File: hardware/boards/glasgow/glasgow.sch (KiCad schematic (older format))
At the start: 95 parts, among them J1 USB_C_USB2.0, SW1 RST, U1 CY7C68013A-56LTX, U15 TPD3S014, U2 CAT24M01X, U3 BL24C256A-SFRC, U30 ICE40HX8K-BG121, U36 TLV73312PQDRVR, U7 APX811-40UG-7, U8 TLV75533PDRVR, Y1 24M

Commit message: revC3: Filled in the blanks for the Reset button part number.
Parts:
- SW1: 1b2-bom-key sw-tact-side-tc-1109de -> sw-tact-side-tc-1109de-b-f; MPN TC-1109DE-X-X -> TC-1109DE-B-F
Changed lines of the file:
@@
 F 3 "https://datasheet.lcsc.com/szlcsc/2006061832_XKB-Connectivity-TC-1109DE-C-G_C400325.pdf" H 8400 4300 50  0001 C CNN
 F 4 "XKB" H 8400 4100 50  0001 C CNN "Mfg"
-F 5 "TC-1109DE-X-X" H 8400 4100 50  0001 C CNN "MPN"
-F 6 "sw-tact-side-tc-1109de" H 8400 4100 50  0001 C CNN "1b2-bom-key"
+F 5 "TC-1109DE-B-F" H 8400 4100 50  0001 C CNN "MPN"
+F 6 "sw-tact-side-tc-1109de-b-f" H 8400 4100 50  0001 C CNN "1b2-bom-key"
 	1    8400 4100
 	-1   0    0    -1

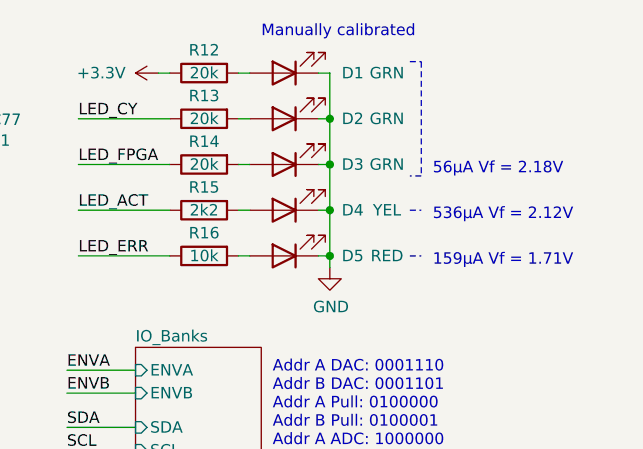
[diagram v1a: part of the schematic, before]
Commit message: revC3: Updated LEDs and current limiting resistors.
* New status LED color scheme: PWR/GRN, FX2/WHT, ICE/BLU, ACT/ORA,
  ERR/RED
* Updated LED part numbers and the corresponding resistor values.
* All LED sourcable from LCSC.
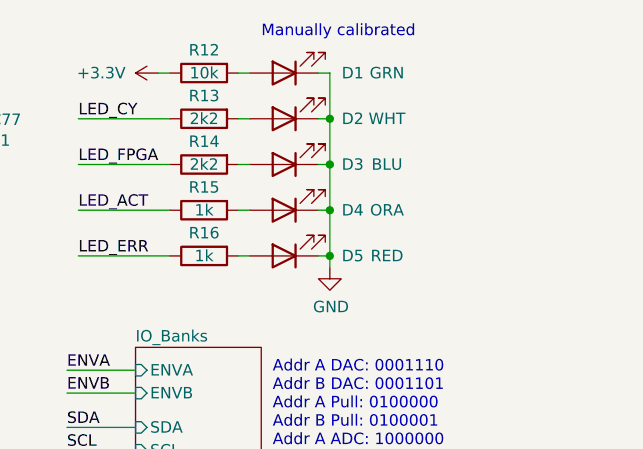
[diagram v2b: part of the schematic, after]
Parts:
- D1: MPN 150060GS75000 -> NCD0603G1; Mfg Wurth Electronics -> Foshan NationStar Optoelectronics
- D2: value GRN -> WHT; 1b2-bom-key led-0603-grn -> led-0603-wht; MPN 150060GS75000 -> NCD0603W1; Mfg Wurth Electronics -> Foshan NationStar Optoelectronics
- D3: value GRN -> BLU; 1b2-bom-key led-0603-grn -> led-0603-blu; MPN 150060GS75000 -> ORH-B36G; Mfg Wurth Electronics -> Orient
- D4: value YEL -> ORA; 1b2-bom-key led-0603-yel -> led-0603-ora; MPN 150060YS75000 -> NCD0603O1; Mfg Wurth Electronics -> Foshan NationStar Optoelectronics
- D5: MPN 150060RS75000 -> NCD0603R1; Mfg Wurth Electronics -> Foshan NationStar Optoelectronics
- R12: value 20k -> 10k; 1b2-bom-key res-0402-20k -> res-0402-10k; MPN RC0402FR-1320KL -> RC0402FR-1310KL
- R13, R14: value 20k -> 2k2; 1b2-bom-key res-0402-20k -> res-0402-2k2; MPN RC0402FR-1320KL -> RC0402FR-132K2L
- R15: value 2k2 -> 1k; 1b2-bom-key res-0402-2k2 -> res-0402-1k; MPN RC0402FR-132K2L -> (none); Mfg Yageo -> (none)
- R16: value 10k -> 1k; 1b2-bom-key res-0402-10k -> res-0402-1k; MPN RC0402FR-1310KL -> (none); Mfg Yageo -> (none)
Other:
- note removed: "159µA Vf = 1.71V"
- note removed: "536µA Vf = 2.12V"
- note removed: "56µA Vf = 2.18V"
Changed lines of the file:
@@
 F 1 "GRN" H 9350 900 50  0000 C CNN
 F 2 "LED_SMD:LED_0603_1608Metric" H 9800 900 50  0001 C CNN
-F 3 "https://www.mouser.com/datasheet/2/445/150060GS75000-368921.pdf" H 9800 900 50  0001 C CNN
-F 4 "Wurth Electronics" H -450 0   50  0001 C CNN "Mfg"
-F 5 "150060GS75000" H -450 0   50  0001 C CNN "MPN"
+F 3 "https://datasheet.lcsc.com/szlcsc/2008201032_Foshan-NationStar-Optoelectronics-NCD0603G1_C84267.pdf" H 9800 900 50  0001 C CNN
+F 4 "Foshan NationStar Optoelectronics" H -450 0   50  0001 C CNN "Mfg"
+F 5 "NCD0603G1" H -450 0   50  0001 C CNN "MPN"
 F 6 "led-0603-grn" H 9800 900 50  0001 C CNN "1b2-bom-key"
 	1    9800 900
@@
 P 9800 1100
 F 0 "D2" H 9500 1100 50  0000 C CNN
-F 1 "GRN" H 9350 1100 50  0000 C CNN
+F 1 "WHT" H 9350 1100 50  0000 C CNN
 F 2 "LED_SMD:LED_0603_1608Metric" H 9800 1100 50  0001 C CNN
-F 3 "https://www.mouser.com/datasheet/2/445/150060GS75000-368921.pdf" H 9800 1100 50  0001 C CNN
-F 4 "Wurth Electronics" H -450 0   50  0001 C CNN "Mfg"
-F 5 "150060GS75000" H -450 0   50  0001 C CNN "MPN"
-F 6 "led-0603-grn" H 9800 1100 50  0001 C CNN "1b2-bom-key"
+F 3 "https://datasheet.lcsc.com/szlcsc/2008201032_Foshan-NationStar-Optoelectronics-NCD0603W1_C84265.pdf" H 9800 1100 50  0001 C CNN
+F 4 "Foshan NationStar Optoelectronics" H -450 0   50  0001 C CNN "Mfg"
+F 5 "NCD0603W1" H -450 0   50  0001 C CNN "MPN"
+F 6 "led-0603-wht" H 9800 1100 50  0001 C CNN "1b2-bom-key"
 	1    9800 1100
 	-1   0    0    1
@@
 P 9800 1300
 F 0 "D3" H 9500 1300 50  0000 C CNN
-F 1 "GRN" H 9350 1300 50  0000 C CNN
+F 1 "BLU" H 9350 1300 50  0000 C CNN
 F 2 "LED_SMD:LED_0603_1608Metric" H 9800 1300 50  0001 C CNN
-F 3 "https://www.mouser.com/datasheet/2/445/150060GS75000-368921.pdf" H 9800 1300 50  0001 C CNN
-F 4 "Wurth Electronics" H -450 0   50  0001 C CNN "Mfg"
-F 5 "150060GS75000" H -450 0   50  0001 C CNN "MPN"
-F 6 "led-0603-grn" H 9800 1300 50  0001 C CNN "1b2-bom-key"
+F 3 "https://datasheet.lcsc.com/szlcsc/1811100911_Orient-ORH-B36G_C193191.pdf" H 9800 1300 50  0001 C CNN
+F 4 "Orient" H -450 0   50  0001 C CNN "Mfg"
+F 5 "ORH-B36G" H -450 0   50  0001 C CNN "MPN"
+F 6 "led-0603-blu" H 9800 1300 50  0001 C CNN "1b2-bom-key"
 	1    9800 1300
 	-1   0    0    1
@@
 P 9800 1500
 F 0 "D4" H 9500 1500 50  0000 C CNN
-F 1 "YEL" H 9350 1500 50  0000 C CNN
+F 1 "ORA" H 9350 1500 50  0000 C CNN
 F 2 "LED_SMD:LED_0603_1608Metric" H 9800 1500 50  0001 C CNN
-F 3 "https://www.mouser.com/datasheet/2/445/150060YS75000-368983.pdf" H 9800 1500 50  0001 C CNN
-F 4 "Wurth Electronics" H -450 0   50  0001 C CNN "Mfg"
-F 5 "150060YS75000" H -450 0   50  0001 C CNN "MPN"
-F 6 "led-0603-yel" H 9800 1500 50  0001 C CNN "1b2-bom-key"
+F 3 "https://datasheet.lcsc.com/szlcsc/2008201033_Foshan-NationStar-Optoelectronics-NCD0603O1_C84269.pdf" H 9800 1500 50  0001 C CNN
+F 4 "Foshan NationStar Optoelectronics" H -450 0   50  0001 C CNN "Mfg"
+F 5 "NCD0603O1" H -450 0   50  0001 C CNN "MPN"
+F 6 "led-0603-ora" H 9800 1500 50  0001 C CNN "1b2-bom-key"
 	1    9800 1500
 	-1   0    0    1
@@
 F 1 "RED" H 9350 1700 50  0000 C CNN
 F 2 "LED_SMD:LED_0603_1608Metric" H 9800 1700 50  0001 C CNN
-F 3 "https://www.mouser.com/datasheet/2/445/150060RS75000-368563.pdf" H 9800 1700 50  0001 C CNN
-F 4 "Wurth Electronics" H -450 0   50  0001 C CNN "Mfg"
-F 5 "150060RS75000" H -450 0   50  0001 C CNN "MPN"
+F 3 "https://datasheet.lcsc.com/szlcsc/2008201032_Foshan-NationStar-Optoelectronics-NCD0603R1_C84263.pdf" H 9800 1700 50  0001 C CNN
+F 4 "Foshan NationStar Optoelectronics" H -450 0   50  0001 C CNN "Mfg"
+F 5 "NCD0603R1" H -450 0   50  0001 C CNN "MPN"
 F 6 "led-0603-red" H 9800 1700 50  0001 C CNN "1b2-bom-key"
 	1    9800 1700
@@
 	1    0    0    -1
 $EndComp
-Wire Notes Line
-	10350 850  10400 850
-Wire Notes Line
-	10400 850  10400 1350
-Wire Notes Line
-	10400 1350 10350 1350
-Text Notes 10450 1350 0    50   ~ 0
-56µA Vf = 2.18V
 $Comp
 L Device:R R12
@@
 P 9450 900
 F 0 "R12" V 9350 900 50  0000 C CNN
-F 1 "20k" V 9450 900 50  0000 C CNN
+F 1 "10k" V 9450 900 50  0000 C CNN
 F 2 "Resistor_SMD:R_0402_1005Metric" V 9380 900 50  0001 C CNN
 F 3 "https://www.mouser.com/datasheet/2/447/PYu-RC_Group_51_RoHS_L_10-1527934.pdf" H 9450 900 50  0001 C CNN
 F 4 "Yageo" H -450 0   50  0001 C CNN "Mfg"
-F 5 "RC0402FR-1320KL" H -450 0   50  0001 C CNN "MPN"
-F 6 "res-0402-20k" H 9450 900 50  0001 C CNN "1b2-bom-key"
+F 5 "RC0402FR-1310KL" H -450 0   50  0001 C CNN "MPN"
+F 6 "res-0402-10k" H 9450 900 50  0001 C CNN "1b2-bom-key"
 	1    9450 900
 	0    -1   1    0
@@
 Wire Wire Line
 	9600 900  9650 900
-Text Notes 10450 1550 0    50   ~ 0
-536µA Vf = 2.12V
 $Comp
 L Device:R R15
@@
 P 9450 1500
 F 0 "R15" V 9350 1500 50  0000 C CNN
-F 1 "2k2" V 9450 1500 50  0000 C CNN
+F 1 "1k" V 9450 1500 50  0000 C CNN
 F 2 "Resistor_SMD:R_0402_1005Metric" V 9380 1500 50  0001 C CNN
-F 3 "https://www.mouser.com/datasheet/2/447/PYu-RC_Group_51_RoHS_L_10-1527934.pdf" H 9450 1500 50  0001 C CNN
-F 4 "Yageo" H -450 0   50  0001 C CNN "Mfg"
-F 5 "RC0402FR-132K2L" H -450 0   50  0001 C CNN "MPN"
-F 6 "res-0402-2k2" H 9450 1500 50  0001 C CNN "1b2-bom-key"
+F 3 "" H 9450 1500 50  0001 C CNN
+F 4 "" H -450 0   50  0001 C CNN "Mfg"
+F 5 "" H -450 0   50  0001 C CNN "MPN"
+F 6 "res-0402-1k" H 9450 1500 50  0001 C CNN "1b2-bom-key"
 	1    9450 1500
 	0    -1   1    0
 $EndComp
-Wire Notes Line
-	10350 1500 10400 1500
-Wire Notes Line
-	10350 1700 10400 1700
 Wire Wire Line
 	9650 1500 9600 1500
@@
 Wire Wire Line
 	9650 1700 9600 1700
-Text Notes 10450 1750 0    50   ~ 0
-159µA Vf = 1.71V
 $Comp
 L Device:R R16
@@
 P 9450 1700
 F 0 "R16" V 9350 1700 50  0000 C CNN
-F 1 "10k" V 9450 1700 50  0000 C CNN
+F 1 "1k" V 9450 1700 50  0000 C CNN
 F 2 "Resistor_SMD:R_0402_1005Metric" V 9380 1700 50  0001 C CNN
-F 3 "https://www.mouser.com/datasheet/2/447/PYu-RC_Group_51_RoHS_L_10-1527934.pdf" H 9450 1700 50  0001 C CNN
-F 4 "Yageo" H -450 0   50  0001 C CNN "Mfg"
-F 5 "RC0402FR-1310KL" H -450 0   50  0001 C CNN "MPN"
-F 6 "res-0402-10k" H 9450 1700 50  0001 C CNN "1b2-bom-key"
+F 3 "" H 9450 1700 50  0001 C CNN
+F 4 "" H -450 0   50  0001 C CNN "Mfg"
+F 5 "" H -450 0   50  0001 C CNN "MPN"
+F 6 "res-0402-1k" H 9450 1700 50  0001 C CNN "1b2-bom-key"
 	1    9450 1700
 	0    -1   1    0
@@
 P 9450 1100
 F 0 "R13" V 9350 1100 50  0000 C CNN
-F 1 "20k" V 9450 1100 50  0000 C CNN
+F 1 "2k2" V 9450 1100 50  0000 C CNN
 F 2 "Resistor_SMD:R_0402_1005Metric" V 9380 1100 50  0001 C CNN
 F 3 "https://www.mouser.com/datasheet/2/447/PYu-RC_Group_51_RoHS_L_10-1527934.pdf" H 9450 1100 50  0001 C CNN
 F 4 "Yageo" H -450 0   50  0001 C CNN "Mfg"
-F 5 "RC0402FR-1320KL" H -450 0   50  0001 C CNN "MPN"
-F 6 "res-0402-20k" H 9450 1100 50  0001 C CNN "1b2-bom-key"
+F 5 "RC0402FR-132K2L" H -450 0   50  0001 C CNN "MPN"
+F 6 "res-0402-2k2" H 9450 1100 50  0001 C CNN "1b2-bom-key"
 	1    9450 1100
 	0    -1   1    0
@@
 P 9450 1300
 F 0 "R14" V 9350 1300 50  0000 C CNN
-F 1 "20k" V 9450 1300 50  0000 C CNN
+F 1 "2k2" V 9450 1300 50  0000 C CNN
 F 2 "Resistor_SMD:R_0402_1005Metric" V 9380 1300 50  0001 C CNN
 F 3 "https://www.mouser.com/datasheet/2/447/PYu-RC_Group_51_RoHS_L_10-1527934.pdf" H 9450 1300 50  0001 C CNN
 F 4 "Yageo" H -450 0   50  0001 C CNN "Mfg"
-F 5 "RC0402FR-1320KL" H -450 0   50  0001 C CNN "MPN"
-F 6 "res-0402-20k" H 9450 1300 50  0001 C CNN "1b2-bom-key"
+F 5 "RC0402FR-132K2L" H -450 0   50  0001 C CNN "MPN"
+F 6 "res-0402-2k2" H 9450 1300 50  0001 C CNN "1b2-bom-key"
 	1    9450 1300
 	0    -1   1    0
